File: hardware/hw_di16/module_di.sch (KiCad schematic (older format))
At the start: 47 parts, among them P1 DEBUG, P2 DI_0, P3 DI_1, P4 MOD_IN, U1 STM32F103C8Tx, U2 TLP291-4

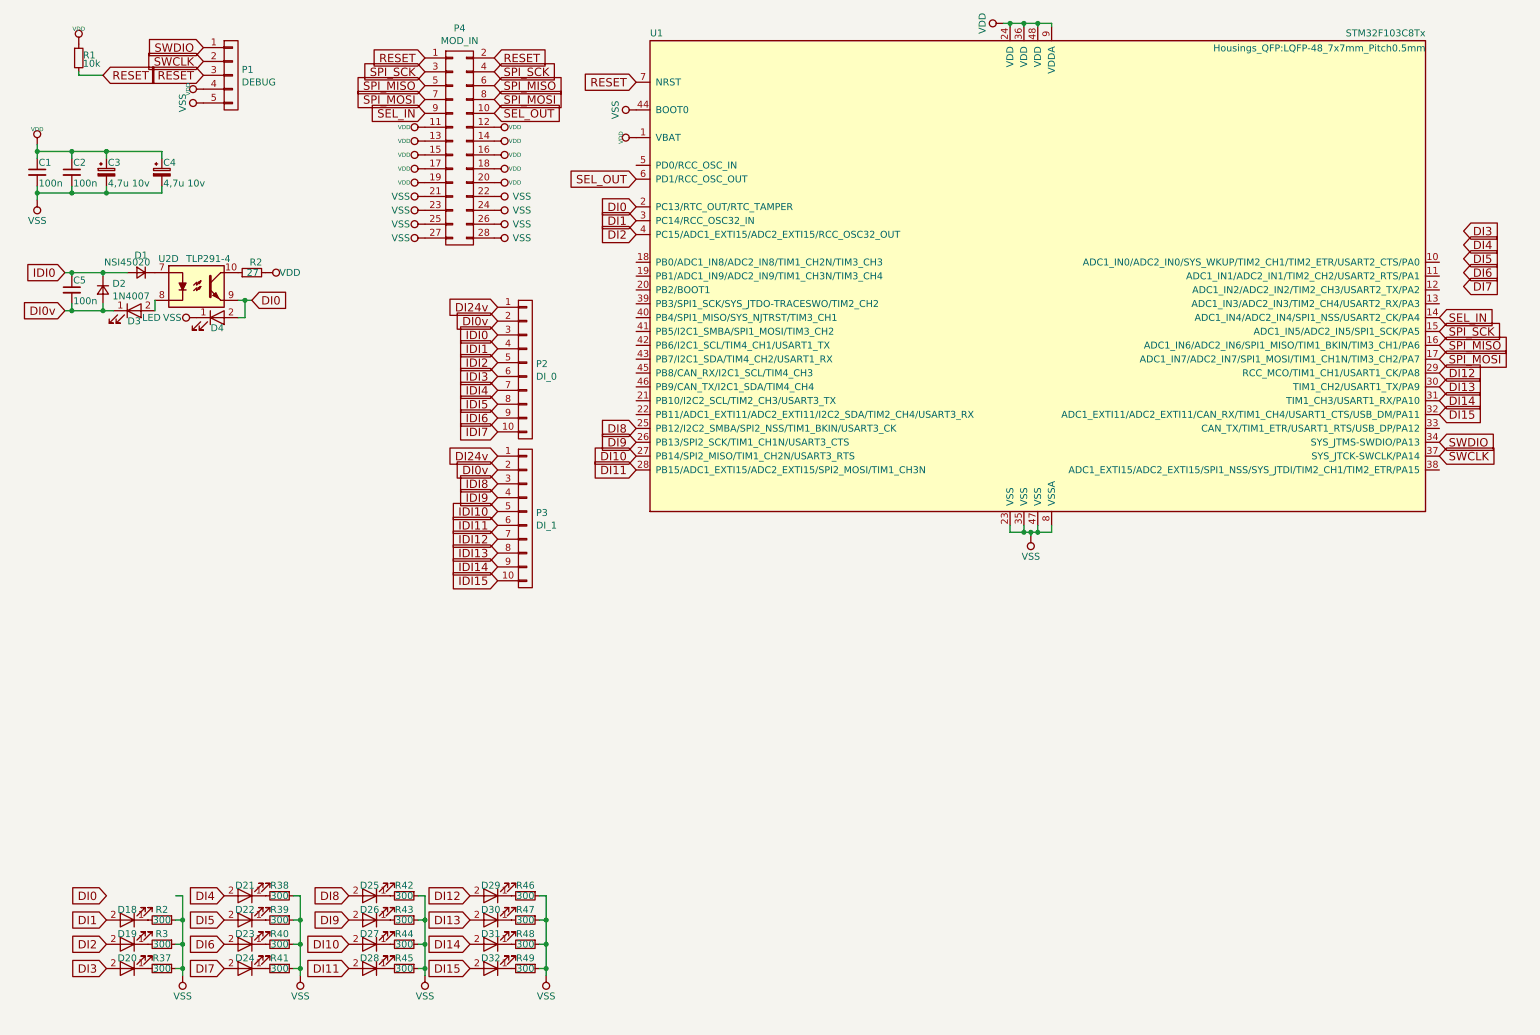
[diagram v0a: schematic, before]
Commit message: Обновлена схема модуля DI16
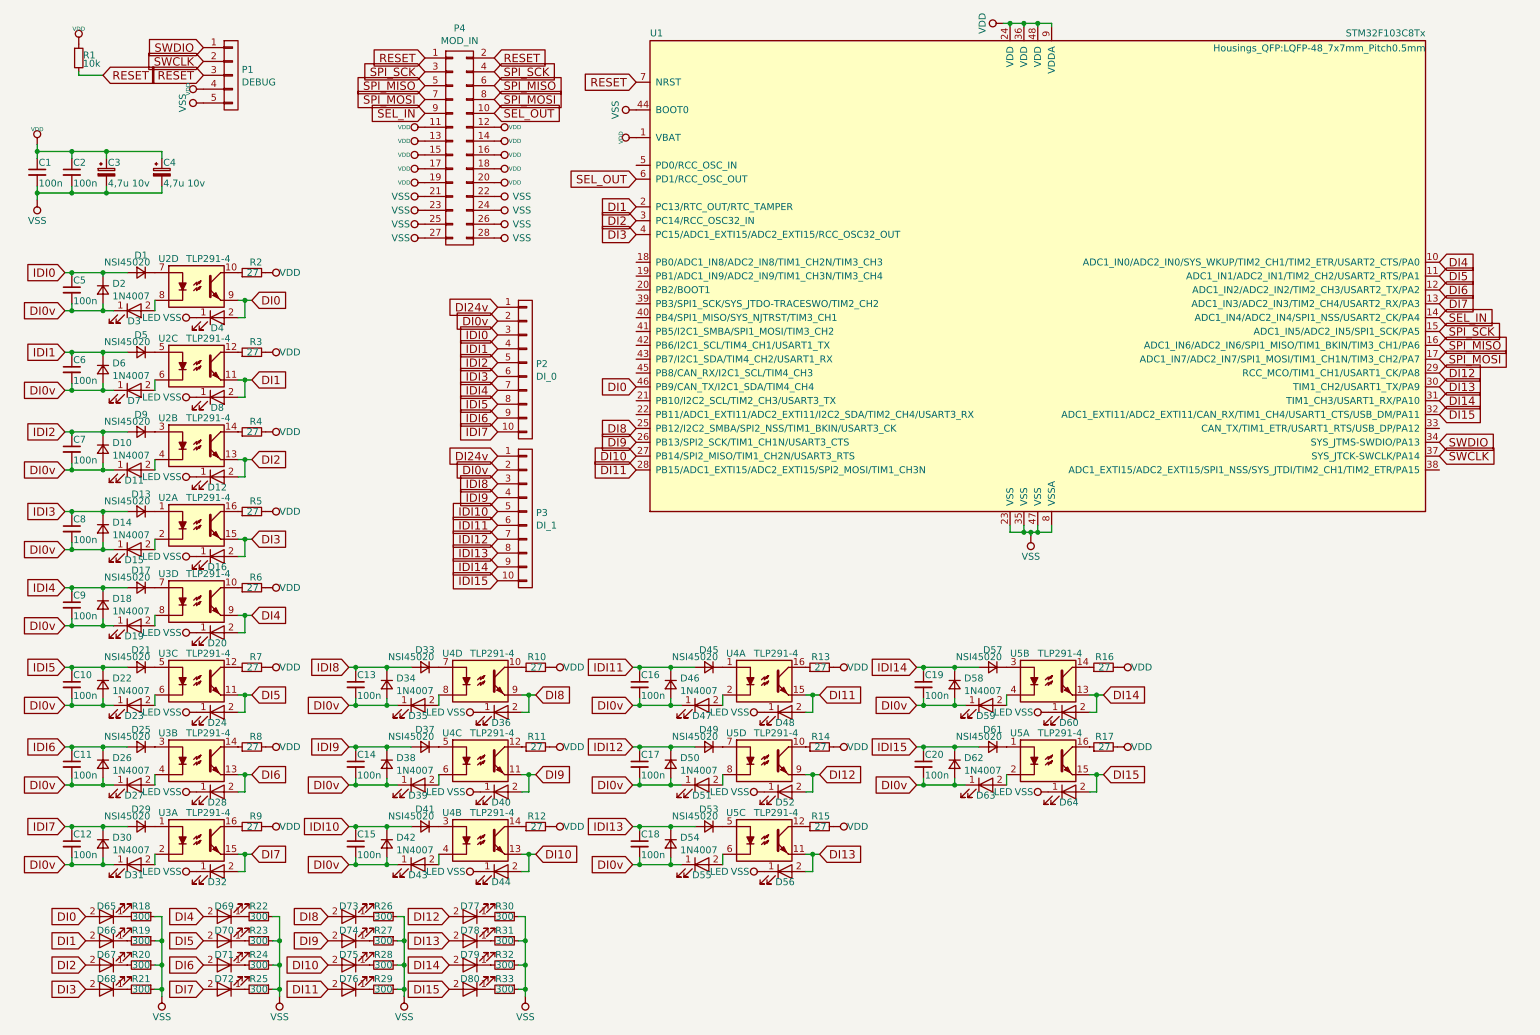
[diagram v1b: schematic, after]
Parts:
- added C10, C11, C12, C13, C14, C15, C16, C17, C18, C19, C20, C6, C7, C8, C9: 100n, Capacitors_SMD:C_0805, symbol C_Small
- added D10, D14, D18, D22, D26, D30, D34, D38, D42, D46, D50, D54, D58, D6, D62: 1N4007, Diodes_SMD:D_SOD-123, symbol D_Small
- added D11, D12, D15, D16, D19, D20, D23, D24, D27, D28, D31, D32, D35, D36, D39, D40, D43, D44, D47, D48, D51, D52, D55, D56, D59, D60, D63, D64, D65, D7, D8: LED, LEDs:LED_0805, symbol LED
- added D13, D17, D21, D25, D29, D33, D37, D41, D45, D49, D5, D53, D57, D61, D9: NSI45020, Diodes_SMD:D_SOD-123, symbol D_Small
- added R10, R11, R12, R13, R14, R15, R16, R17, R3, R4, R5, R6, R7, R8, R9: 27, Resistors_SMD:R_0805, symbol R_Small
- added R18: 300, Resistors_SMD:R_0805, symbol R_Small
- added unit 3 of U2
- added unit 2 of U2
- added unit 1 of U2
- added U3, U4, U5: TLP291-4, SMD_Packages:SO-16-N, symbol TLP291-4
- D2: footprint (none) -> Diodes_SMD:D_SOD-123
- D3, D4: footprint (none) -> LEDs:LED_0805
- D66: renamed from D18; footprint (none) -> LEDs:LED_0805
- D67: renamed from D19; footprint (none) -> LEDs:LED_0805
- D68: renamed from D20; footprint (none) -> LEDs:LED_0805
- D69: renamed from D21; footprint (none) -> LEDs:LED_0805
- D70: renamed from D22; footprint (none) -> LEDs:LED_0805
- D71: renamed from D23; footprint (none) -> LEDs:LED_0805
- D72: renamed from D24; footprint (none) -> LEDs:LED_0805
- D73: renamed from D25; footprint (none) -> LEDs:LED_0805
- D74: renamed from D26; footprint (none) -> LEDs:LED_0805
- D75: renamed from D27; footprint (none) -> LEDs:LED_0805
- D76: renamed from D28; footprint (none) -> LEDs:LED_0805
- D77: renamed from D29; footprint (none) -> LEDs:LED_0805
- D78: renamed from D30; footprint (none) -> LEDs:LED_0805
- D79: renamed from D31; footprint (none) -> LEDs:LED_0805
- D80: renamed from D32; footprint (none) -> LEDs:LED_0805
- R19: renamed from R2; footprint (none) -> Resistors_SMD:R_0805
- R20: renamed from R3; footprint (none) -> Resistors_SMD:R_0805
- R21: renamed from R37; footprint (none) -> Resistors_SMD:R_0805
- R22: renamed from R38; footprint (none) -> Resistors_SMD:R_0805
- R23: renamed from R39; footprint (none) -> Resistors_SMD:R_0805
- R24: renamed from R40; footprint (none) -> Resistors_SMD:R_0805
- R25: renamed from R41; footprint (none) -> Resistors_SMD:R_0805
- R26: renamed from R42; footprint (none) -> Resistors_SMD:R_0805
- R27: renamed from R43; footprint (none) -> Resistors_SMD:R_0805
- R28: renamed from R44; footprint (none) -> Resistors_SMD:R_0805
- R29: renamed from R45; footprint (none) -> Resistors_SMD:R_0805
- R30: renamed from R46; footprint (none) -> Resistors_SMD:R_0805
- R31: renamed from R47; footprint (none) -> Resistors_SMD:R_0805
- R32: renamed from R48; footprint (none) -> Resistors_SMD:R_0805
- R33: renamed from R49; footprint (none) -> Resistors_SMD:R_0805
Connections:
- net DI0: now also U1.46 (PB9/CAN_TX/I2C1_SDA/TIM4_CH4), D65.2 (A); no longer U1.2 (PC13/RTC_OUT/RTC_TAMPER)
- net DI0v: now also C10.2, C11.2, C12.2, C13.2, C14.2, C15.2, C16.2, C17.2, C18.2, C19.2, C20.2, C6.2, C7.2, C8.2, C9.2, D10.2 (A), D11.1 (K), D14.2 (A), D15.1 (K), D18.2 (A), D19.1 (K), D22.2 (A), D23.1 (K), D26.2 (A), D27.1 (K), D30.2 (A), D31.1 (K), D34.2 (A), D35.1 (K), D38.2 (A), D39.1 (K), D42.2 (A), D43.1 (K), D46.2 (A), D47.1 (K), D50.2 (A), D51.1 (K), D54.2 (A), D55.1 (K), D58.2 (A), D59.1 (K), D6.2 (A), D62.2 (A), D63.1 (K), D7.1 (K)
- net DI1: now also U1.2 (PC13/RTC_OUT/RTC_TAMPER), D8.2 (A), U2.11; no longer U1.3 (PC14/RCC_OSC32_IN)
- net DI10: now also D44.2 (A), U4.13
- net DI11: now also D48.2 (A), U4.15
- net DI12: now also D52.2 (A), U5.9
- net DI13: now also D56.2 (A), U5.11
- net DI14: now also D60.2 (A), U5.13
- net DI15: now also D64.2 (A), U5.15
- net DI2: now also U1.3 (PC14/RCC_OSC32_IN), D12.2 (A), U2.13; no longer U1.4 (PC15/ADC1_EXTI15/ADC2_EXTI15/RCC_OSC32_OUT)
- net DI3: now also U1.4 (PC15/ADC1_EXTI15/ADC2_EXTI15/RCC_OSC32_OUT), D16.2 (A), U2.15
- net DI4: now also U1.10 (ADC1_IN0/ADC2_IN0/SYS_WKUP/TIM2_CH1/TIM2_ETR/USART2_CTS/PA0), D20.2 (A), U3.9
- net DI5: now also U1.11 (ADC1_IN1/ADC2_IN1/TIM2_CH2/USART2_RTS/PA1), D24.2 (A), U3.11
- net DI6: now also U1.12 (ADC1_IN2/ADC2_IN2/TIM2_CH3/USART2_TX/PA2), D28.2 (A), U3.13
- net DI7: now also U1.13 (ADC1_IN3/ADC2_IN3/TIM2_CH4/USART2_RX/PA3), D32.2 (A), U3.15
- net DI8: now also D36.2 (A), U4.9
- net DI9: now also D40.2 (A), U4.11
- net IDI1: now also C6.1, D5.2 (A), D6.1 (K)
- net IDI10: now also C15.1, D41.2 (A), D42.1 (K)
- net IDI11: now also C16.1, D45.2 (A), D46.1 (K)
- net IDI12: now also C17.1, D49.2 (A), D50.1 (K)
- net IDI13: now also C18.1, D53.2 (A), D54.1 (K)
- net IDI14: now also C19.1, D57.2 (A), D58.1 (K)
- net IDI15: now also C20.1, D61.2 (A), D62.1 (K)
- net IDI2: now also C7.1, D10.1 (K), D9.2 (A)
- net IDI3: now also C8.1, D13.2 (A), D14.1 (K)
- net IDI4: now also C9.1, D17.2 (A), D18.1 (K)
- net IDI5: now also C10.1, D21.2 (A), D22.1 (K)
- net IDI6: now also C11.1, D25.2 (A), D26.1 (K)
- net IDI7: now also C12.1, D29.2 (A), D30.1 (K)
- net IDI8: now also C13.1, D33.2 (A), D34.1 (K)
- net IDI9: now also C14.1, D37.2 (A), D38.1 (K)
- net VDD: now also R10.2, R11.2, R12.2, R13.2, R14.2, R15.2, R16.2, R17.2, R3.2, R4.2, R5.2, R6.2, R7.2, R8.2, R9.2
- net VSS: now also D12.1 (K), D16.1 (K), D20.1 (K), D24.1 (K), D28.1 (K), D32.1 (K), D36.1 (K), D40.1 (K), D44.1 (K), D48.1 (K), D52.1 (K), D56.1 (K), D60.1 (K), D64.1 (K), D8.1 (K), R18.1
- new net: R3.1, U2.12
- new net: D5.1 (K), U2.5
- new net: D7.2 (A), U2.6
- new net: R4.1, U2.14
- new net: D9.1 (K), U2.3
- new net: D11.2 (A), U2.4
- new net: D13.1 (K), U2.1
- new net: R5.1, U2.16
- new net: D15.2 (A), U2.2
- new net: R6.1, U3.10
- new net: D17.1 (K), U3.7
- new net: D19.2 (A), U3.8
- new net: R7.1, U3.12
- new net: D21.1 (K), U3.5
- new net: D23.2 (A), U3.6
- new net: R8.1, U3.14
- new net: D25.1 (K), U3.3
- new net: D27.2 (A), U3.4
- new net: D29.1 (K), U3.1
- new net: R9.1, U3.16
- new net: D31.2 (A), U3.2
- new net: R10.1, U4.10
- new net: D33.1 (K), U4.7
- new net: D35.2 (A), U4.8
- new net: R11.1, U4.12
- new net: D37.1 (K), U4.5
- new net: D39.2 (A), U4.6
- new net: R12.1, U4.14
- new net: D41.1 (K), U4.3
- new net: D43.2 (A), U4.4
- new net: D45.1 (K), U4.1
- new net: R13.1, U4.16
- new net: D47.2 (A), U4.2
- new net: R14.1, U5.10
- new net: D49.1 (K), U5.7
- new net: D51.2 (A), U5.8
- new net: R15.1, U5.12
- new net: D53.1 (K), U5.5
- new net: D55.2 (A), U5.6
- new net: R16.1, U5.14
- new net: D57.1 (K), U5.3
- new net: D59.2 (A), U5.4
- new net: D61.1 (K), U5.1
- new net: R17.1, U5.16
- new net: D63.2 (A), U5.2
- new net: D65.1 (K), R18.2
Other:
- moved on the sheet: D66, D67, D68, D69, D70, D71, D72, D73, D74, D75, D76, D77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

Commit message: Обновлена схема модуля DI16
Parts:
- P4: footprint (none) -> Projects:Pin_Header_2.00mm_SMD
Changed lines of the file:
@@
 F 0 "P4" H 3650 2290 50  0000 C CNN
 F 1 "MOD_IN" H 3650 2199 50  0000 C CNN
-F 2 "" H 3650 275 50  0001 C CNN
+F 2 "Projects:Pin_Header_2.00mm_SMD" H 3650 275 50  0001 C CNN
 F 3 "" H 3650 275 50  0001 C CNN
 	1    3650 1425
